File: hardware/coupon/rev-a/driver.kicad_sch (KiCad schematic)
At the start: 7 parts, among them U1 TLC59581RTQT

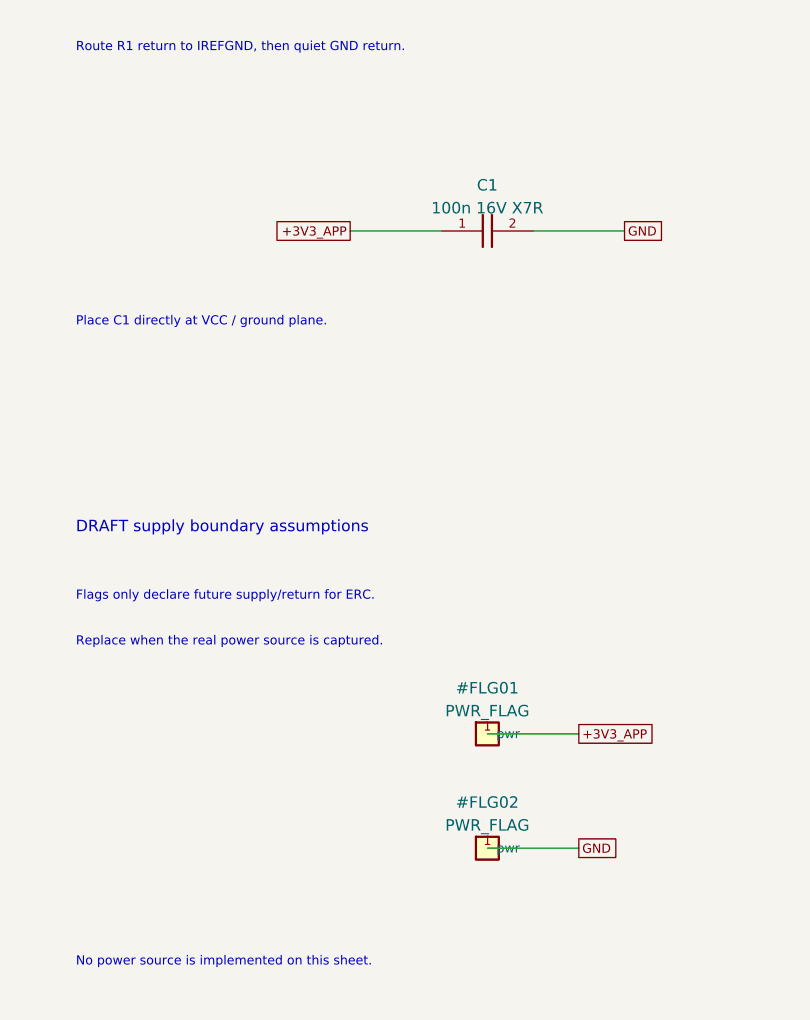
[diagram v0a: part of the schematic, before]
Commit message: Connect driver readback to a probe pad and record native ERC finding
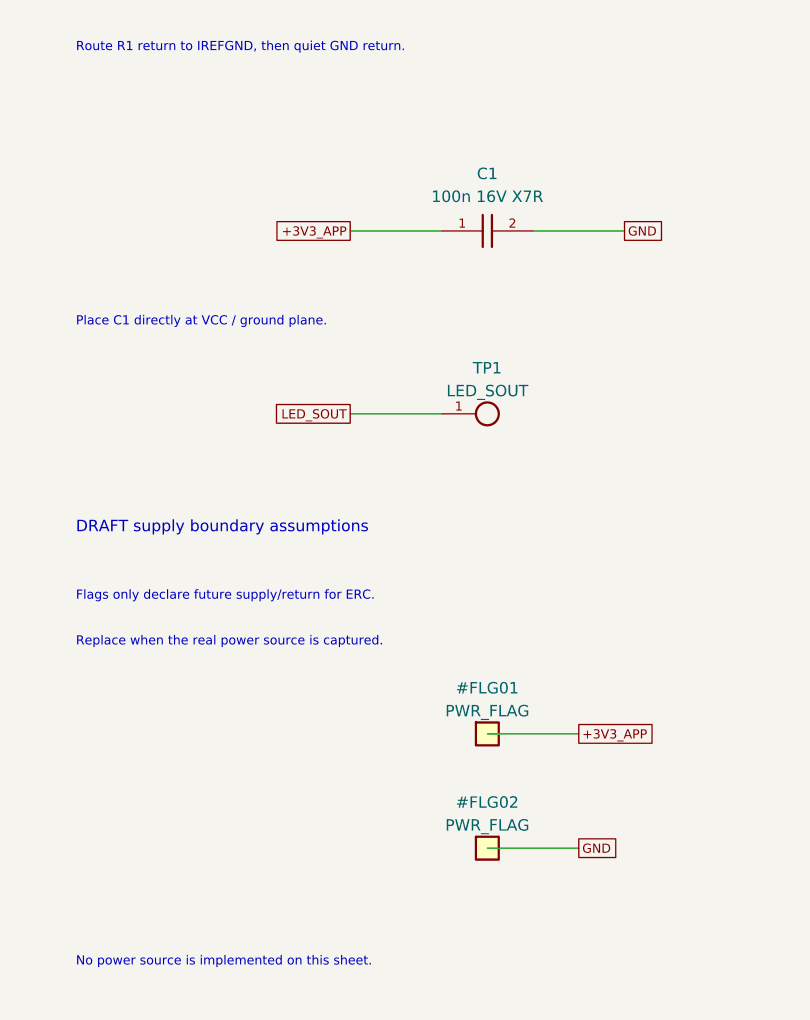
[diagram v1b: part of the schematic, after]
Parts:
- added TP1: LED_SOUT, rgb-badge-coupon:TestPoint_Pad_D1.0mm, symbol rgb-badge-coupon:TestPoint_Pad
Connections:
- net LED_SOUT: now also TP1.1
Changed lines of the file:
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@@
 (global_label "GND" (shape passive) (at 284.480 66.040 0) (effects (font (size 1.016 1.016)) (justify left)) (property "Intersheetrefs" "${INTERSHEET_REFS}" (at 284.480 66.040 0) (effects (font (size 1.27 1.27)) (hide yes))) )
 (symbol (lib_id "rgb-badge-coupon:GRM155R71C104KA88D") (at 269.24 96.52 0) (unit 1) (exclude_from_sim no) (in_bom yes) (on_board yes) (dnp no)
-(property "Reference" "C1" (at 269.240 91.440 0) (effects (font (size 1.27 1.27))))
-(property "Value" "100n 16V X7R" (at 269.240 93.980 0) (effects (font (size 1.27 1.27))))
+(property "Reference" "C1" (at 269.240 90.170 0) (effects (font (size 1.27 1.27))))
+(property "Value" "100n 16V X7R" (at 269.240 92.710 0) (effects (font (size 1.27 1.27))))
 (property "Footprint" "rgb-badge-coupon:C_Murata_GRM15_0402" (at 269.240 96.520 0) (effects (font (size 1.27 1.27)) (hide yes)))
 (property "Datasheet" "https://pim.murata.com/asset/pim4/ceramicCapacitorSMD/GRM155R71C104KA88-01A-EN_PDF_CERAMICCAPACITORSMD" (at 269.240 96.520 0) (effects (font (size 1.27 1.27)) (hide yes)))
@@
 (text "100k logic defaults" (at 317.5 48.26 0) (effects (font (size 1.27 1.27)) (justify left)))
 (text "Pull-downs do not replace row / VLED inhibit." (at 223.52 190.5 0) (effects (font (size 1.016 1.016)) (justify left)))
+(symbol (lib_id "rgb-badge-coupon:TestPoint_Pad") (at 269.24 116.84 0) (unit 1) (exclude_from_sim no) (in_bom no) (on_board yes) (dnp no)
+(property "Reference" "TP1" (at 269.240 111.760 0) (effects (font (size 1.27 1.27))))
+(property "Value" "LED_SOUT" (at 269.240 114.300 0) (effects (font (size 1.27 1.27))))
+(property "Footprint" "rgb-badge-coupon:TestPoint_Pad_D1.0mm" (at 269.240 116.840 0) (effects (font (size 1.27 1.27)) (hide yes)))
+(property "Datasheet" "" (at 269.240 116.840 0) (effects (font (size 1.27 1.27)) (hide yes)))
+(property "Manufacturer" "PCB copper feature" (at 269.240 116.840 0) (effects (font (size 1.27 1.27)) (hide yes)))
+(property "MPN" "" (at 269.240 116.840 0) (effects (font (size 1.27 1.27)) (hide yes)))
+(pin "1")
+(instances (project "rgb-badge-coupon" (path "/207fb68e-2ddb-46bb-8712-eba2f8c5eef6/28db03d9-d0db-503e-aef0-5aceaf14cea3" (reference "TP1") (unit 1)))))
+(wire (pts (xy 264.160 116.840) (xy 254.000 116.840)) (stroke (width 0) (type default)))
+(global_label "LED_SOUT" (shape passive) (at 254.000 116.840 180) (effects (font (size 1.016 1.016)) (justify right)) (property "Intersheetrefs" "${INTERSHEET_REFS}" (at 254.000 116.840 0) (effects (font (size 1.27 1.27)) (hide yes))))
 (embedded_fonts no)
 )

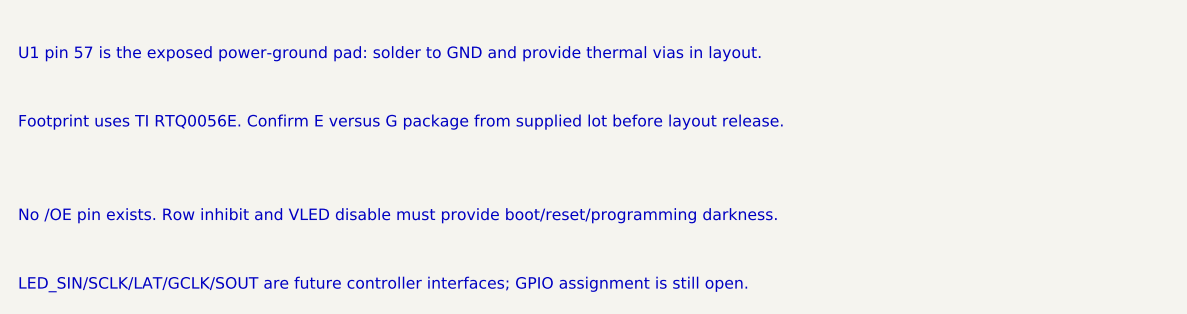
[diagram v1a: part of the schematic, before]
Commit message: Accept corrected power-library review and clear row schematic title block
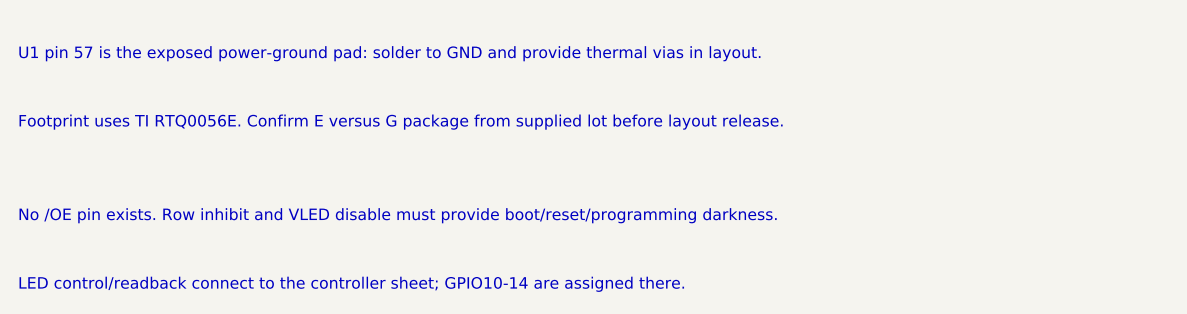
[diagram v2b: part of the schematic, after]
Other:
- note added: "LED control/readback connect to the controller sheet; GPIO10-14 are assigned there."
- note removed: "LED_SIN/SCLK/LAT/GCLK/SOUT are future controller interfaces; GPIO assignment is still open."
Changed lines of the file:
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@@
 (kicad_sch (version 20260306) (generator "rgb_badge") (paper "A3")
-(title_block (title "Coupon Rev A - TLC59581 driver") (rev "A-draft") (comment 1 "SPDX-License-Identifier: CERN-OHL-S-2.0") (comment 2 "Draft: controller, row inhibit and power source pending"))
+(title_block (title "Coupon Rev A - TLC59581 driver") (rev "A-draft") (comment 1 "SPDX-License-Identifier: CERN-OHL-S-2.0") (comment 2 "Controller/rows captured; VLED interlock and power pending"))
 (symbol (lib_id "rgb-badge-coupon:TLC59581RTQT") (at 132.08 116.84 0) (unit 1) (exclude_from_sim no) (in_bom yes) (on_board yes) (dnp no)
 (property "Reference" "U1" (at 132.080 48.260 0) (effects (font (size 1.27 1.27))))
@@
 (text "Footprint uses TI RTQ0056E. Confirm E versus G package from supplied lot before layout release." (at 20.32 228.6 0) (effects (font (size 1.27 1.27)) (justify left)))
 (text "No /OE pin exists. Row inhibit and VLED disable must provide boot/reset/programming darkness." (at 20.32 239 0) (effects (font (size 1.27 1.27)) (justify left)))
-(text "LED_SIN/SCLK/LAT/GCLK/SOUT are future controller interfaces; GPIO assignment is still open." (at 20.32 246.62 0) (effects (font (size 1.27 1.27)) (justify left)))
+(text "LED control/readback connect to the controller sheet; GPIO10-14 are assigned there." (at 20.32 246.62 0) (effects (font (size 1.27 1.27)) (justify left)))
 (symbol (lib_id "rgb-badge-coupon:ERJ-2RKF1003X") (at 350.52 66.04 0) (unit 1) (exclude_from_sim no) (in_bom yes) (on_board yes) (dnp no)
 (property "Reference" "R2" (at 350.520 60.960 0) (effects (font (size 1.27 1.27))))

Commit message: Normalize Panasonic ERJ order codes across coupon
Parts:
- R1: symbol rgb-badge-coupon:ERJ-2RKF3922X -> rgb-badge-coupon:ERJ2RKF3922X; MPN ERJ-2RKF3922X -> ERJ2RKF3922X
- R2, R3, R4, R5: symbol rgb-badge-coupon:ERJ-2RKF1003X -> rgb-badge-coupon:ERJ2RKF1003X; MPN ERJ-2RKF1003X -> ERJ2RKF1003X
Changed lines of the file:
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@@
 (wire (pts (xy 109.220 167.640) (xy 99.060 167.640)) (stroke (width 0) (type default)))
 (global_label "GND" (shape passive) (at 99.060 167.640 180) (effects (font (size 1.016 1.016)) (justify right)) (property "Intersheetrefs" "${INTERSHEET_REFS}" (at 99.060 167.640 0) (effects (font (size 1.27 1.27)) (hide yes))) )
-(symbol (lib_id "rgb-badge-coupon:ERJ-2RKF3922X") (at 269.24 66.04 0) (unit 1) (exclude_from_sim no) (in_bom yes) (on_board yes) (dnp no)
+(symbol (lib_id "rgb-badge-coupon:ERJ2RKF3922X") (at 269.24 66.04 0) (unit 1) (exclude_from_sim no) (in_bom yes) (on_board yes) (dnp no)
 (property "Reference" "R1" (at 269.240 60.960 0) (effects (font (size 1.27 1.27))))
 (property "Value" "39.2k 1%" (at 269.240 63.500 0) (effects (font (size 1.27 1.27))))
@@
 (property "Datasheet" "https://industrial.panasonic.com/cdbs/www-data/pdf/RDA0000/AOA0000C304.pdf" (at 269.240 66.040 0) (effects (font (size 1.27 1.27)) (hide yes)))
 (property "Manufacturer" "Panasonic" (at 269.240 66.040 0) (effects (font (size 1.27 1.27)) (hide yes)))
-(property "MPN" "ERJ-2RKF3922X" (at 269.240 66.040 0) (effects (font (size 1.27 1.27)) (hide yes)))
+(property "MPN" "ERJ2RKF3922X" (at 269.240 66.040 0) (effects (font (size 1.27 1.27)) (hide yes)))
 (pin "1")
 (pin "2")
@@
 (text "No /OE pin exists. Row inhibit and VLED disable must provide boot/reset/programming darkness." (at 20.32 239 0) (effects (font (size 1.27 1.27)) (justify left)))
 (text "LED control/readback connect to the controller sheet; GPIO10-14 are assigned there." (at 20.32 246.62 0) (effects (font (size 1.27 1.27)) (justify left)))
-(symbol (lib_id "rgb-badge-coupon:ERJ-2RKF1003X") (at 350.52 66.04 0) (unit 1) (exclude_from_sim no) (in_bom yes) (on_board yes) (dnp no)
+(symbol (lib_id "rgb-badge-coupon:ERJ2RKF1003X") (at 350.52 66.04 0) (unit 1) (exclude_from_sim no) (in_bom yes) (on_board yes) (dnp no)
 (property "Reference" "R2" (at 350.520 60.960 0) (effects (font (size 1.27 1.27))))
 (property "Value" "100k 1%" (at 350.520 63.500 0) (effects (font (size 1.27 1.27))))
@@
 (property "Datasheet" "https://industrial.panasonic.com/cdbs/www-data/pdf/RDA0000/AOA0000C304.pdf" (at 350.520 66.040 0) (effects (font (size 1.27 1.27)) (hide yes)))
 (property "Manufacturer" "Panasonic" (at 350.520 66.040 0) (effects (font (size 1.27 1.27)) (hide yes)))
-(property "MPN" "ERJ-2RKF1003X" (at 350.520 66.040 0) (effects (font (size 1.27 1.27)) (hide yes)))
+(property "MPN" "ERJ2RKF1003X" (at 350.520 66.040 0) (effects (font (size 1.27 1.27)) (hide yes)))
 (pin "1")
 (pin "2")
@@
 (wire (pts (xy 355.600 66.040) (xy 365.760 66.040)) (stroke (width 0) (type default)))
 (global_label "GND" (shape passive) (at 365.760 66.040 0) (effects (font (size 1.016 1.016)) (justify left)) (property "Intersheetrefs" "${INTERSHEET_REFS}" (at 365.760 66.040 0) (effects (font (size 1.27 1.27)) (hide yes))) )
-(symbol (lib_id "rgb-badge-coupon:ERJ-2RKF1003X") (at 350.52 96.52 0) (unit 1) (exclude_from_sim no) (in_bom yes) (on_board yes) (dnp no)
+(symbol (lib_id "rgb-badge-coupon:ERJ2RKF1003X") (at 350.52 96.52 0) (unit 1) (exclude_from_sim no) (in_bom yes) (on_board yes) (dnp no)
 (property "Reference" "R3" (at 350.520 91.440 0) (effects (font (size 1.27 1.27))))
 (property "Value" "100k 1%" (at 350.520 93.980 0) (effects (font (size 1.27 1.27))))
@@
 (property "Datasheet" "https://industrial.panasonic.com/cdbs/www-data/pdf/RDA0000/AOA0000C304.pdf" (at 350.520 96.520 0) (effects (font (size 1.27 1.27)) (hide yes)))
 (property "Manufacturer" "Panasonic" (at 350.520 96.520 0) (effects (font (size 1.27 1.27)) (hide yes)))
-(property "MPN" "ERJ-2RKF1003X" (at 350.520 96.520 0) (effects (font (size 1.27 1.27)) (hide yes)))
+(property "MPN" "ERJ2RKF1003X" (at 350.520 96.520 0) (effects (font (size 1.27 1.27)) (hide yes)))
 (pin "1")
 (pin "2")
@@
 (wire (pts (xy 355.600 96.520) (xy 365.760 96.520)) (stroke (width 0) (type default)))
 (global_label "GND" (shape passive) (at 365.760 96.520 0) (effects (font (size 1.016 1.016)) (justify left)) (property "Intersheetrefs" "${INTERSHEET_REFS}" (at 365.760 96.520 0) (effects (font (size 1.27 1.27)) (hide yes))) )
-(symbol (lib_id "rgb-badge-coupon:ERJ-2RKF1003X") (at 350.52 127.0 0) (unit 1) (exclude_from_sim no) (in_bom yes) (on_board yes) (dnp no)
+(symbol (lib_id "rgb-badge-coupon:ERJ2RKF1003X") (at 350.52 127.0 0) (unit 1) (exclude_from_sim no) (in_bom yes) (on_board yes) (dnp no)
 (property "Reference" "R4" (at 350.520 121.920 0) (effects (font (size 1.27 1.27))))
 (property "Value" "100k 1%" (at 350.520 124.460 0) (effects (font (size 1.27 1.27))))
@@
 (property "Datasheet" "https://industrial.panasonic.com/cdbs/www-data/pdf/RDA0000/AOA0000C304.pdf" (at 350.520 127.000 0) (effects (font (size 1.27 1.27)) (hide yes)))
 (property "Manufacturer" "Panasonic" (at 350.520 127.000 0) (effects (font (size 1.27 1.27)) (hide yes)))
-(property "MPN" "ERJ-2RKF1003X" (at 350.520 127.000 0) (effects (font (size 1.27 1.27)) (hide yes)))
+(property "MPN" "ERJ2RKF1003X" (at 350.520 127.000 0) (effects (font (size 1.27 1.27)) (hide yes)))
 (pin "1")
 (pin "2")
@@
 (wire (pts (xy 355.600 127.000) (xy 365.760 127.000)) (stroke (width 0) (type default)))
 (global_label "GND" (shape passive) (at 365.760 127.000 0) (effects (font (size 1.016 1.016)) (justify left)) (property "Intersheetrefs" "${INTERSHEET_REFS}" (at 365.760 127.000 0) (effects (font (size 1.27 1.27)) (hide yes))) )
-(symbol (lib_id "rgb-badge-coupon:ERJ-2RKF1003X") (at 350.52 157.48 0) (unit 1) (exclude_from_sim no) (in_bom yes) (on_board yes) (dnp no)
+(symbol (lib_id "rgb-badge-coupon:ERJ2RKF1003X") (at 350.52 157.48 0) (unit 1) (exclude_from_sim no) (in_bom yes) (on_board yes) (dnp no)
 (property "Reference" "R5" (at 350.520 152.400 0) (effects (font (size 1.27 1.27))))
 (property "Value" "100k 1%" (at 350.520 154.940 0) (effects (font (size 1.27 1.27))))
@@
 (property "Datasheet" "https://industrial.panasonic.com/cdbs/www-data/pdf/RDA0000/AOA0000C304.pdf" (at 350.520 157.480 0) (effects (font (size 1.27 1.27)) (hide yes)))
 (property "Manufacturer" "Panasonic" (at 350.520 157.480 0) (effects (font (size 1.27 1.27)) (hide yes)))
-(property "MPN" "ERJ-2RKF1003X" (at 350.520 157.480 0) (effects (font (size 1.27 1.27)) (hide yes)))
+(property "MPN" "ERJ2RKF1003X" (at 350.520 157.480 0) (effects (font (size 1.27 1.27)) (hide yes)))
 (pin "1")
 (pin "2")

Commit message: Connect provisional app switch and 3V3 converter
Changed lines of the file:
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@@
 (wire (pts (xy 274.320 96.520) (xy 284.480 96.520)) (stroke (width 0) (type default)))
 (global_label "GND" (shape passive) (at 284.480 96.520 0) (effects (font (size 1.016 1.016)) (justify left)) (property "Intersheetrefs" "${INTERSHEET_REFS}" (at 284.480 96.520 0) (effects (font (size 1.27 1.27)) (hide yes))) )
-(symbol (lib_id "rgb-badge-coupon:PWR_FLAG") (at 269.24 152.4 0) (unit 1) (exclude_from_sim no) (in_bom no) (on_board no) (dnp no)
-(property "Reference" "#FLG01" (at 269.240 147.320 0) (effects (font (size 1.27 1.27))))
-(property "Value" "PWR_FLAG" (at 269.240 149.860 0) (effects (font (size 1.27 1.27))))
-(property "Footprint" "" (at 269.240 152.400 0) (effects (font (size 1.27 1.27)) (hide yes)))
-(property "Datasheet" "" (at 269.240 152.400 0) (effects (font (size 1.27 1.27)) (hide yes)))
-(property "Manufacturer" "" (at 269.240 152.400 0) (effects (font (size 1.27 1.27)) (hide yes)))
-(property "MPN" "" (at 269.240 152.400 0) (effects (font (size 1.27 1.27)) (hide yes)))
-(pin "1")
-(instances (project "rgb-badge-coupon" (path "/207fb68e-2ddb-46bb-8712-eba2f8c5eef6/28db03d9-d0db-503e-aef0-5aceaf14cea3" (reference "#FLG01") (unit 1)))))
-(wire (pts (xy 269.240 152.400) (xy 279.400 152.400)) (stroke (width 0) (type default)))
-(global_label "+3V3_APP" (shape passive) (at 279.400 152.400 0) (effects (font (size 1.016 1.016)) (justify left)) (property "Intersheetrefs" "${INTERSHEET_REFS}" (at 279.400 152.400 0) (effects (font (size 1.27 1.27)) (hide yes))) )
 (symbol (lib_id "rgb-badge-coupon:PWR_FLAG") (at 269.24 165.1 0) (unit 1) (exclude_from_sim no) (in_bom no) (on_board no) (dnp no)
 (property "Reference" "#FLG02" (at 269.240 160.020 0) (effects (font (size 1.27 1.27))))
